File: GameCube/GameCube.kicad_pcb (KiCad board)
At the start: 2 copper layers, 1 part, among them U2 ESP32-DevKitC

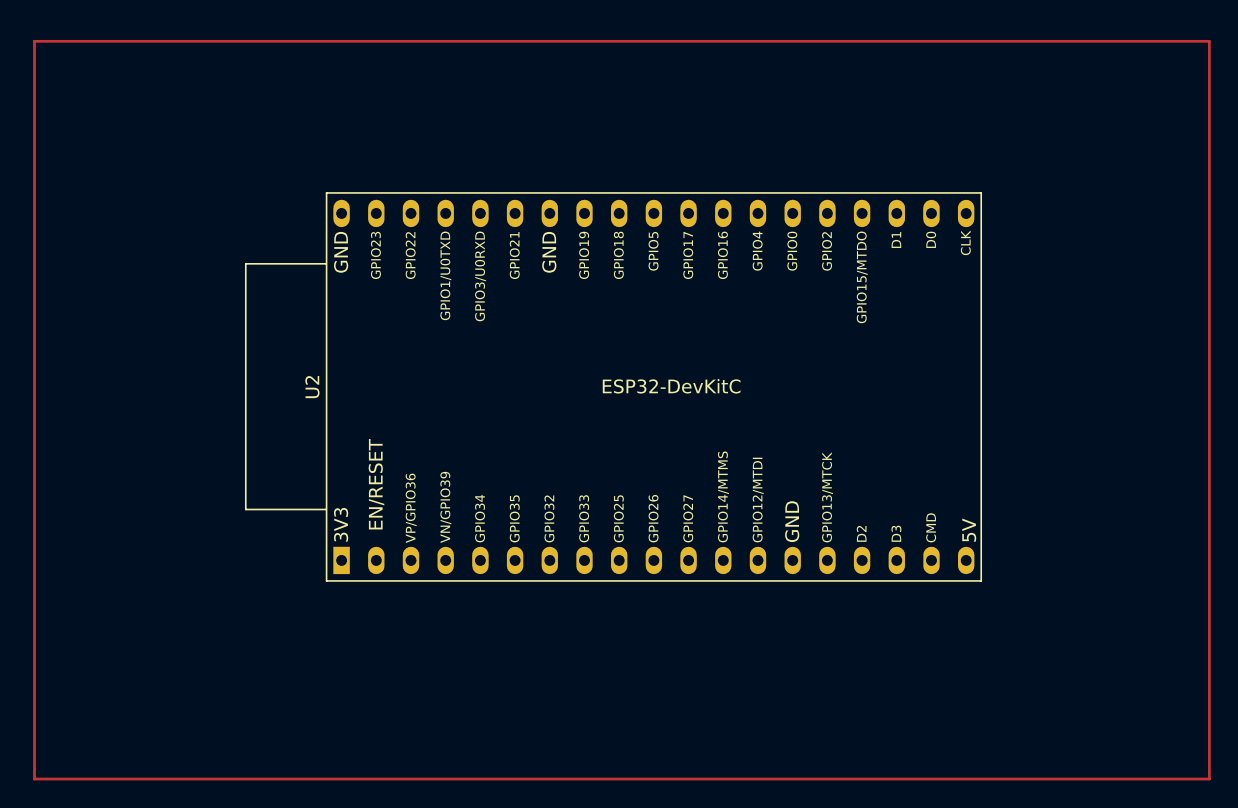
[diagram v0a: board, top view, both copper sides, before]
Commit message: Add footprints and rough layout
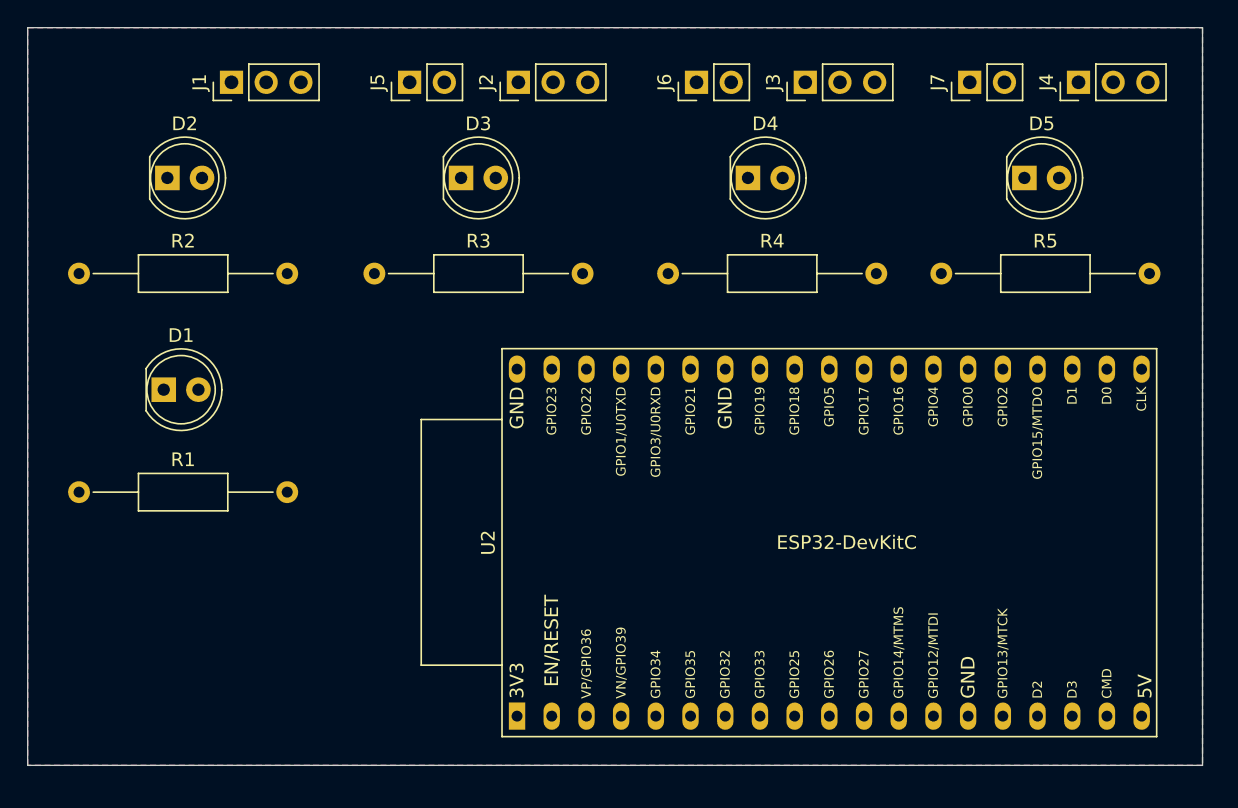
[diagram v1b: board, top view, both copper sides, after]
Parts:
- added D1: LED, LED_THT:LED_D5.0mm, F.Cu at (111.0, 89.0)
- added D2: LED, LED_THT:LED_D5.0mm, F.Cu at (111.2, 73.5)
- added D3: LED, LED_THT:LED_D5.0mm, F.Cu at (132.7, 73.5)
- added D4: LED, LED_THT:LED_D5.0mm, F.Cu at (153.7, 73.5)
- added D5: LED, LED_THT:LED_D5.0mm, F.Cu at (174.0, 73.5)
- added J1: Conn_01x03_Pin, Connector_PinHeader_2.54mm:PinHeader_1x03_P2.54mm_Vertical, F.Cu at (115.9, 66.5)
- added J2: Conn_01x03_Pin, Connector_PinHeader_2.54mm:PinHeader_1x03_P2.54mm_Vertical, F.Cu at (136.9, 66.5)
- added J3: Conn_01x03_Pin, Connector_PinHeader_2.54mm:PinHeader_1x03_P2.54mm_Vertical, F.Cu at (157.9, 66.5)
- added J4: Conn_01x03_Pin, Connector_PinHeader_2.54mm:PinHeader_1x03_P2.54mm_Vertical, F.Cu at (177.9, 66.5)
- added J5: Conn_01x02_Pin, Connector_PinHeader_2.54mm:PinHeader_1x02_P2.54mm_Vertical, F.Cu at (129.0, 66.5)
- added J6: Conn_01x02_Pin, Connector_PinHeader_2.54mm:PinHeader_1x02_P2.54mm_Vertical, F.Cu at (150.0, 66.5)
- added J7: Conn_01x02_Pin, Connector_PinHeader_2.54mm:PinHeader_1x02_P2.54mm_Vertical, F.Cu at (170.0, 66.5)
- added R1: R, Resistor_THT:R_Axial_DIN0207_L6.3mm_D2.5mm_P15.24mm_Horizontal, F.Cu at (104.8, 96.5)
- added R2: R, Resistor_THT:R_Axial_DIN0207_L6.3mm_D2.5mm_P15.24mm_Horizontal, F.Cu at (104.8, 80.5)
- added R3: R, Resistor_THT:R_Axial_DIN0207_L6.3mm_D2.5mm_P15.24mm_Horizontal, F.Cu at (126.4, 80.5)
- added R4: R, Resistor_THT:R_Axial_DIN0207_L6.3mm_D2.5mm_P15.24mm_Horizontal, F.Cu at (147.9, 80.5)
- added R5: R, Resistor_THT:R_Axial_DIN0207_L6.3mm_D2.5mm_P15.24mm_Horizontal, F.Cu at (167.9, 80.5)
- moved U2 17.2 mm to (136.8, 112.9)
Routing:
- added copper zone on B.Cu, net GND
- added copper zone on F.Cu, net GND
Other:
- board outline added: 86 x 54 mm
